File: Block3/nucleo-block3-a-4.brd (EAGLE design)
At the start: 100.3 x 80 mm, 90 parts, among them IC2 TL331, J4 MODJACK6P6C-MJ3245-66-0CONN_M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, J5 MODJACK6P6C-MJ3245-66-0CONN_M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, Q1 NPN-23, Q3 BSS84, Q4 BSS123, U1 TC4428ACOA, U2 TC4428ACOA, U3 TC4428ACOA

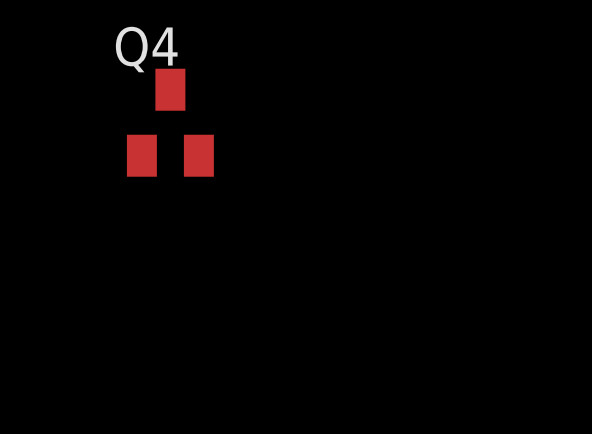
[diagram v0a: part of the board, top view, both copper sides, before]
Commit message: rearranges schematic sheets.
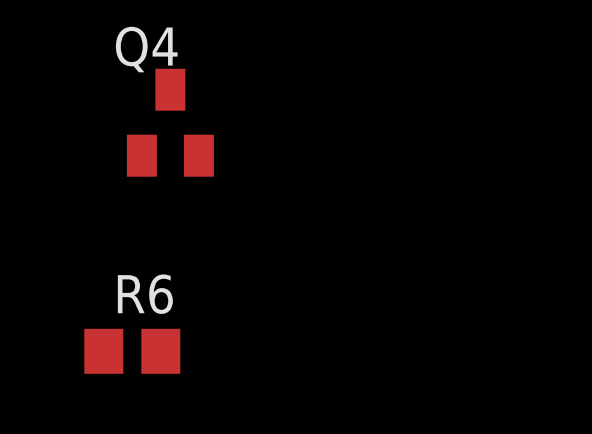
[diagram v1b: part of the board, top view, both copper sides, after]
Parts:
- added R6: 47k, rcl:R0805
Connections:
- net GND: now also R6.1
- net LN-TX-P: now also R6.2
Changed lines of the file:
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@@
 <attribute name="VALUE" x="-128.905" y="-659.765" size="1.27" layer="27"/>
+</element>
+<element name="R6" library="rcl" library_urn="urn:adsk.eagle:library:334" package="R0805" package3d_urn="urn:adsk.eagle:package:23553/2" value="47k" x="-128.27" y="-664.21" smashed="yes">
+<attribute name="NAME" x="-128.905" y="-662.94" size="1.27" layer="25"/>
+<attribute name="POPULARITY" value="86" x="-128.27" y="-664.21" size="1.778" layer="27" display="off"/>
+<attribute name="SPICEPREFIX" value="R" x="-128.27" y="-664.21" size="1.778" layer="27" display="off"/>
+<attribute name="VALUE" x="-128.905" y="-666.75" size="1.27" layer="27"/>
 </element>
 </elements>
@@
 <contactref element="Q4" pad="2"/>
 <contactref element="JP1" pad="5"/>
+<contactref element="R6" pad="1"/>
 <wire x1="-112.5" y1="-399.08" x2="-103.4" y2="-399.07" width="0" layer="19" extent="1-1"/>
 <wire x1="-112.5" y1="-388.92" x2="-112.5" y2="-399.08" width="0" layer="19" extent="1-1"/>
@@
 <wire x1="0" y1="-585.47" x2="-103.4" y2="-505.75" width="0" layer="19" extent="1-1"/>
 <wire x1="-126.05" y1="-657.69" x2="0" y2="-585.47" width="0" layer="19" extent="1-1"/>
+<wire x1="-129.22" y1="-664.21" x2="-126.05" y2="-657.69" width="0" layer="19" extent="1-1"/>
 <wire x1="-20.35" y1="-74.19" x2="-66.0908" y2="-220.09" width="0" layer="19" extent="1-1"/>
 <wire x1="-15.27" y1="-74.19" x2="-20.35" y2="-74.19" width="0" layer="19" extent="1-1"/>
@@
 <contactref element="G1" pad="PC5"/>
 <contactref element="Q4" pad="1"/>
+<contactref element="R6" pad="2"/>
 <wire x1="-127.95" y1="-657.69" x2="81.28" y2="67.31" width="0" layer="19" extent="1-1"/>
+<wire x1="-127.32" y1="-664.21" x2="-127.95" y2="-657.69" width="0" layer="19" extent="1-1"/>
 </signal>
 <signal name="LN-TX-B">

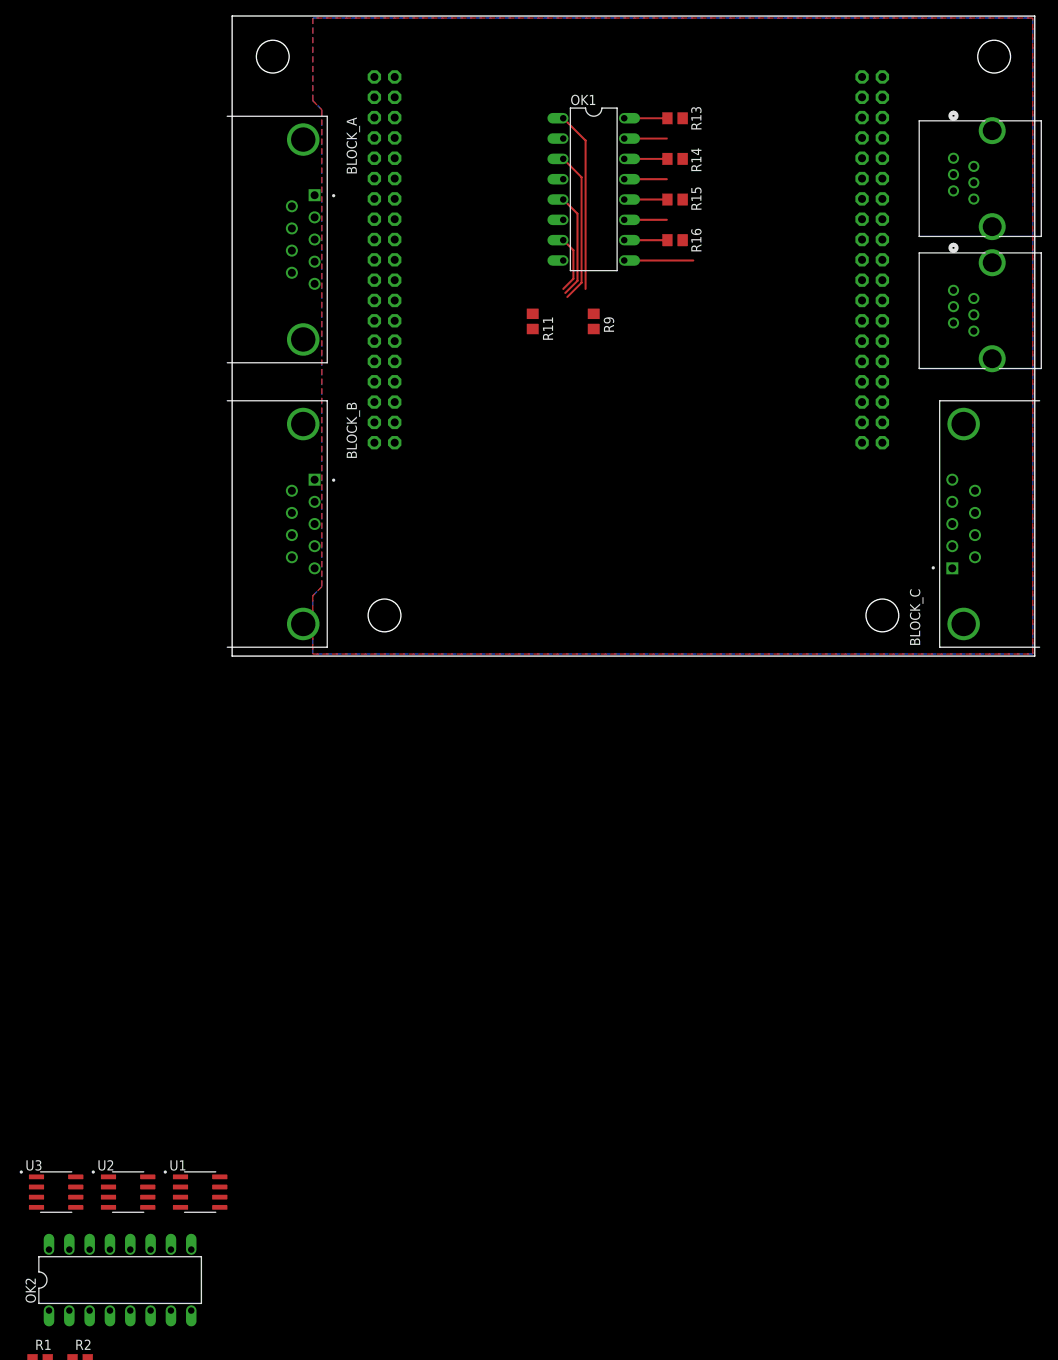
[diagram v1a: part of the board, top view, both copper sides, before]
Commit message: Rearranges gates of the optocouplers.
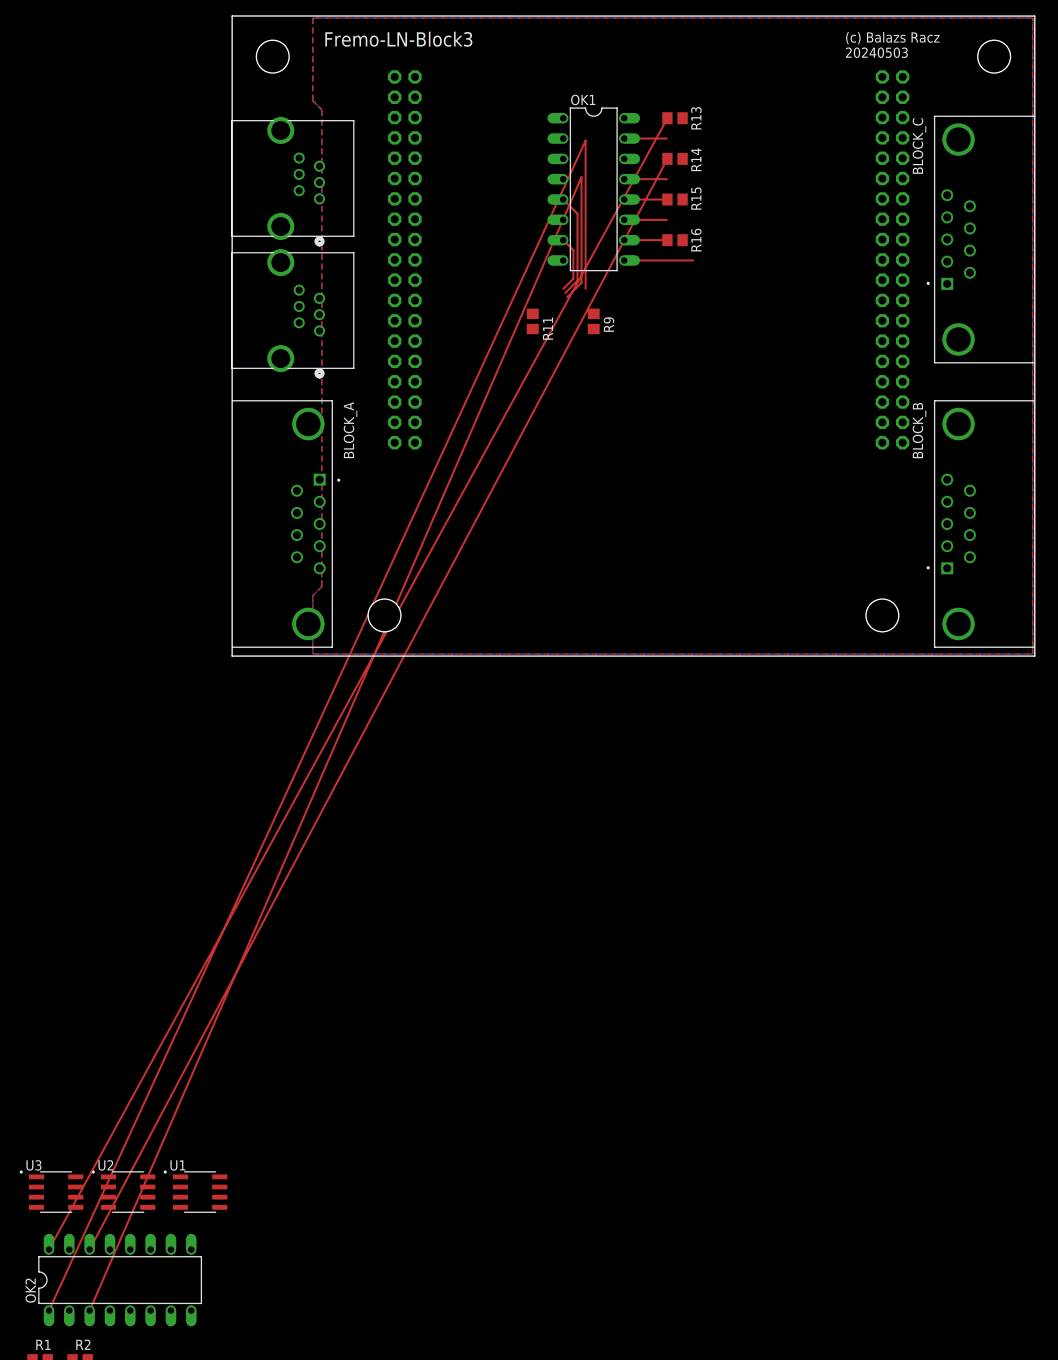
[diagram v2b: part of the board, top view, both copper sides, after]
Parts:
- moved J4 82.1 mm to (10.9, 40.6), turned to 270 degrees
- moved BLOCK_B 81.9 mm to (90.8, 16.5), turned to 90 degrees
- moved J5 80.1 mm to (10.9, 57.1), turned to 270 degrees
- moved BLOCK_A 35.6 mm to (9.53, 16.5)
- moved BLOCK_C 35.6 mm to (90.8, 52.1)
- moved G1 2.54 mm to (20.3, 26.7)
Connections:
- net BLKA-RX-: now also OK2.2, OK2.3; no longer OK1.2, OK1.3
- net BLKC-RX-: now also OK1.2, OK1.3; no longer OK2.2, OK2.3
- net N$1: now also OK1.1, OK1.4; no longer OK2.1, OK2.4
- net N$2: now also OK1.16; no longer OK2.16
- net N$3: now also OK1.14; no longer OK2.14
- net N$31: now also OK2.1, OK2.4; no longer OK1.1, OK1.4
- net N$41: now also OK2.16; no longer OK1.16
- net N$42: now also OK2.14; no longer OK1.14
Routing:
- net N$31: track 22.5 -> 179.4 mm
- net N$41: track 5.40 -> 161.2 mm
- net BLKA-RX-: track 19.0 -> 170.2 mm
- net N$42: track 5.40 -> 154.3 mm
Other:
- board text added: "(c) Balazs Racz 20240503"
- board text added: ">REVISION"
- board text added: "Fremo-LN-Block3"
- board text removed: "(c) Balazs Racz 20230604"
- board text removed: "Signaladapter"

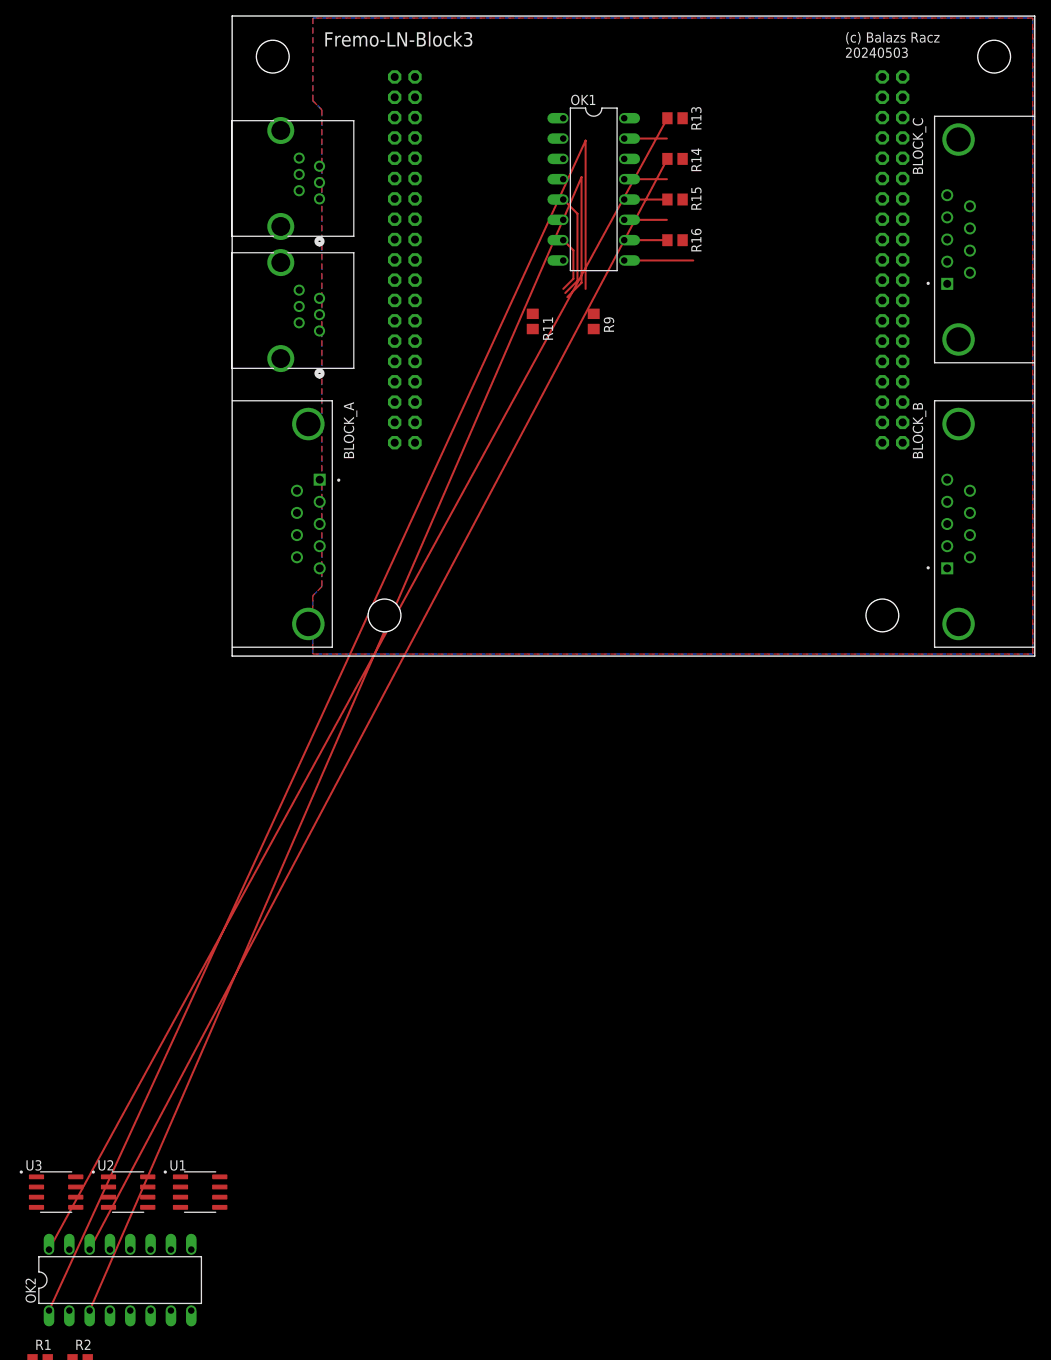
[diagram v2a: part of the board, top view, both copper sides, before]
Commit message: Removes the ground planes for now.
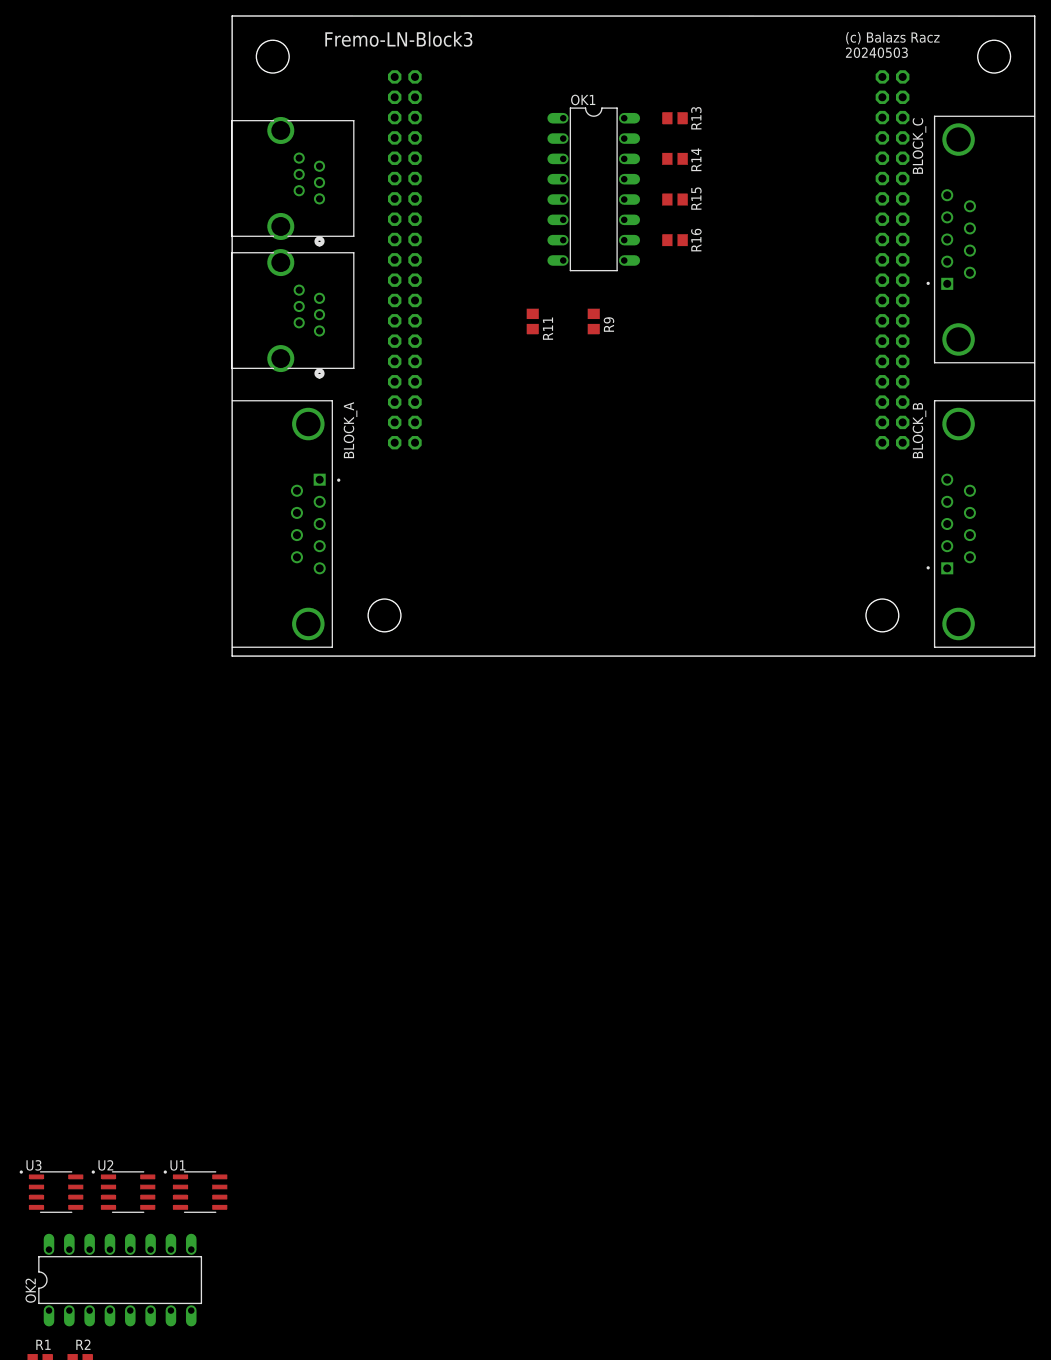
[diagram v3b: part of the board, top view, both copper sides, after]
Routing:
- net N$31: track 179.4 -> 0.00 mm
- net BLKA-RX-: track 170.2 -> 0.00 mm
- net N$41: track 161.2 -> 0.00 mm
- net N$42: track 154.3 -> 0.00 mm
- net GND: track 24.6 -> 0.00 mm
- net N$35: track 13.1 -> 0.00 mm
- net BLKB-RX-: track 7.15 -> 0.00 mm
- net N$44: track 5.40 -> 0.00 mm
- net N$43: track 5.40 -> 0.00 mm
- removed copper zone on layer 1, net GND
- removed copper zone on layer 16, net GND
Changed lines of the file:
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@@
 <signals>
 <signal name="GND">
-<polygon width="0.0762" layer="16" isolate="0.254">
-<vertex x="100.076" y="79.756"/>
-<vertex x="100.076" y="0.254"/>
-<vertex x="10.082" y="0.254"/>
-<vertex x="10.082" y="7.542"/>
-<vertex x="11.21" y="8.67"/>
-<vertex x="11.21" y="68.292"/>
-<vertex x="10.082" y="69.42"/>
-<vertex x="10.082" y="79.756"/>
-</polygon>
-<polygon width="0.0762" layer="1" isolate="0.254">
-<vertex x="100.076" y="0.254"/>
-<vertex x="100.076" y="79.756"/>
-<vertex x="10.082" y="79.756"/>
-<vertex x="10.082" y="69.42"/>
-<vertex x="11.21" y="68.292"/>
-<vertex x="11.21" y="8.67"/>
-<vertex x="10.082" y="7.542"/>
-<vertex x="10.082" y="0.254"/>
-</polygon>
 <contactref element="U1" pad="3"/>
 <contactref element="U2" pad="3"/>
 <contactref element="U3" pad="3"/>
-<wire x1="49.01" y1="64.69" x2="54.344" y2="64.69" width="0.254" layer="1"/>
-<wire x1="49.01" y1="59.61" x2="54.344" y2="59.61" width="0.254" layer="1"/>
 <contactref element="OK1" pad="11"/>
-<wire x1="49.01" y1="54.53" x2="54.344" y2="54.53" width="0.254" layer="1"/>
 <contactref element="OK1" pad="9"/>
-<wire x1="57.646" y1="49.45" x2="49.01" y2="49.45" width="0.254" layer="1"/>
 <contactref element="G1" pad="GND4"/>
 <contactref element="G1" pad="GND5"/>
@@
 <wire x1="49.01" y1="49.45" x2="22.86" y2="49.53" width="0" layer="19" extent="1-1"/>
 <wire x1="49.01" y1="54.53" x2="49.01" y2="49.45" width="0" layer="19" extent="1-1"/>
-<wire x1="54.344" y1="59.61" x2="54.344" y2="54.53" width="0" layer="19" extent="1-1"/>
-<wire x1="54.344" y1="64.69" x2="54.344" y2="59.61" width="0" layer="19" extent="1-1"/>
-<wire x1="83.82" y1="49.53" x2="57.646" y2="49.45" width="0" layer="19" extent="1-1"/>
+<wire x1="49.01" y1="59.61" x2="49.01" y2="54.53" width="0" layer="19" extent="1-1"/>
+<wire x1="49.01" y1="64.69" x2="49.01" y2="59.61" width="0" layer="19" extent="1-1"/>
+<wire x1="83.82" y1="49.53" x2="49.01" y2="49.45" width="0" layer="19" extent="1-1"/>
 <wire x1="83.82" y1="34.29" x2="83.82" y2="49.53" width="0" layer="19" extent="1-1"/>
 </signal>
 <signal name="N$31">
 <contactref element="R9" pad="1"/>
-<wire x1="44.184" y1="45.894" x2="44.184" y2="64.436" width="0.254" layer="1"/>
-<wire x1="44.184" y1="64.436" x2="-22.89" y2="-81.81" width="0.254" layer="1"/>
 <contactref element="OK2" pad="1"/>
 <contactref element="OK2" pad="4"/>
-<wire x1="-22.89" y1="-81.81" x2="-15.27" y2="-81.81" width="0" layer="19" extent="1-1"/>
-<wire x1="45.2" y1="42.78" x2="44.184" y2="45.894" width="0" layer="19" extent="1-1"/>
+<wire x1="-15.27" y1="-81.81" x2="-22.89" y2="-81.81" width="0" layer="19" extent="1-1"/>
+<wire x1="45.2" y1="42.78" x2="-15.27" y2="-81.81" width="0" layer="19" extent="1-1"/>
 </signal>
 <signal name="BLKA-RX-">
-<wire x1="41.898" y1="44.878" x2="43.676" y2="46.656" width="0.254" layer="1"/>
-<wire x1="43.676" y1="46.656" x2="43.676" y2="59.864" width="0.254" layer="1"/>
-<wire x1="43.676" y1="59.864" x2="-17.81" y2="-81.81" width="0.254" layer="1"/>
 <contactref element="BLOCK_A" pad="4"/>
 <contactref element="OK2" pad="2"/>
 <contactref element="OK2" pad="3"/>
 <wire x1="-17.81" y1="-81.81" x2="-20.35" y2="-81.81" width="0" layer="19" extent="1-1"/>
-<wire x1="10.945" y1="13.74" x2="41.898" y2="44.878" width="0" layer="19" extent="1-1"/>
+<wire x1="10.945" y1="13.74" x2="-17.81" y2="-81.81" width="0" layer="19" extent="1-1"/>
 </signal>
 <signal name="N$35">
 <contactref element="R11" pad="1"/>
 <contactref element="OK1" pad="5"/>
-<wire x1="41.644" y1="45.386" x2="43.168" y2="46.91" width="0.254" layer="1"/>
-<wire x1="43.168" y1="55.292" x2="41.39" y2="57.07" width="0.254" layer="1"/>
-<wire x1="43.168" y1="46.91" x2="43.168" y2="55.292" width="0.254" layer="1"/>
 <contactref element="OK1" pad="8"/>
-<wire x1="41.644" y1="45.386" x2="41.39" y2="49.45" width="0" layer="19" extent="16-16"/>
-<wire x1="37.58" y1="42.78" x2="41.644" y2="45.386" width="0" layer="19" extent="16-16"/>
+<wire x1="41.39" y1="49.45" x2="41.39" y2="57.07" width="0" layer="19" extent="1-1"/>
+<wire x1="37.58" y1="42.78" x2="41.39" y2="49.45" width="0" layer="19" extent="1-1"/>
 </signal>
 <signal name="BLKB-RX-">
 <contactref element="OK1" pad="7"/>
-<wire x1="41.39" y1="45.894" x2="42.66" y2="47.164" width="0.254" layer="1"/>
-<wire x1="42.66" y1="47.164" x2="42.66" y2="50.72" width="0.254" layer="1"/>
-<wire x1="42.66" y1="50.72" x2="41.39" y2="51.99" width="0.254" layer="1"/>
 <contactref element="OK1" pad="6"/>
 <contactref element="BLOCK_B" pad="4"/>
-<wire x1="41.39" y1="51.99" x2="41.39" y2="54.53" width="0" layer="19" extent="1-1"/>
-<wire x1="89.385" y1="19.28" x2="41.39" y2="45.894" width="0" layer="19" extent="16-16"/>
+<wire x1="41.39" y1="51.99" x2="89.385" y2="19.28" width="0" layer="19" extent="1-1"/>
+<wire x1="41.39" y1="54.53" x2="41.39" y2="51.99" width="0" layer="19" extent="1-1"/>
 </signal>
 <signal name="N$41">
 <contactref element="R13" pad="2"/>
-<wire x1="54.41" y1="67.23" x2="-22.89" y2="-74.19" width="0.254" layer="1"/>
 <contactref element="OK2" pad="16"/>
+<wire x1="-22.89" y1="-74.19" x2="54.41" y2="67.23" width="0" layer="19" extent="1-1"/>
 </signal>
 <signal name="N$42">
 <contactref element="R14" pad="2"/>
-<wire x1="54.41" y1="62.15" x2="-17.81" y2="-74.19" width="0.254" layer="1"/>
 <contactref element="OK2" pad="14"/>
+<wire x1="-17.81" y1="-74.19" x2="54.41" y2="62.15" width="0" layer="19" extent="1-1"/>
 </signal>
 <signal name="N$43">
 <contactref element="R15" pad="2"/>
 <contactref element="OK1" pad="12"/>
-<wire x1="54.41" y1="57.07" x2="49.01" y2="57.07" width="0.254" layer="1"/>
+<wire x1="49.01" y1="57.07" x2="54.41" y2="57.07" width="0" layer="19" extent="1-1"/>
 </signal>
 <signal name="N$44">
 <contactref element="R16" pad="2"/>
 <contactref element="OK1" pad="10"/>
-<wire x1="54.41" y1="51.99" x2="49.01" y2="51.99" width="0.254" layer="1"/>
+<wire x1="49.01" y1="51.99" x2="54.41" y2="51.99" width="0" layer="19" extent="1-1"/>
 </signal>
 <signal name="BLKA-RX+">
